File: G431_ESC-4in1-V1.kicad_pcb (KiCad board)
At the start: 4 copper layers, 46 x 55.8 mm, 223 parts, among them J1 Conn_01x02, J10 Conn_01x03, J11 Conn_01x03, J2 Conn_01x10, J3 Conn_01x04, J4 Conn_01x04, J5 Conn_01x04, J6 Conn_01x03, J7 Conn_01x04, J8 Conn_01x03, J9 Conn_01x10, Q1 TPH1R204PB, Q10 TPH1R204PB, Q11 TPH1R204PB, Q12 TPH1R204PB, Q13 TPH1R204PB, Q14 TPH1R204PB, Q15 TPH1R204PB, Q16 TPH1R204PB, Q17 TPH1R204PB, Q18 TPH1R204PB, Q19 TPH1R204PB, Q2 TPH1R204PB, Q20 TPH1R204PB, Q21 TPH1R204PB, Q22 TPH1R204PB, Q23 TPH1R204PB, Q24 TPH1R204PB, Q3 TPH1R204PB, Q4 TPH1R204PB, Q5 TPH1R204PB, Q6 TPH1R204PB, Q7 TPH1R204PB, Q8 TPH1R204PB, Q9 TPH1R204PB, U1 FD6288Q, U10 FD6288Q, U11 FD6288Q, U12 STM32G431KBU6, U13 L78L12_SOT89, U14 MP4560_QFN10, U15 DTOM, U2 STM32G431KBU6, U3 L78L12_SOT89, U4 LP2985-3.3, U5 INA139, U6 STM32G431KBU6, U7 OPA340NA, U8 FD6288Q, U9 STM32G431KBU6

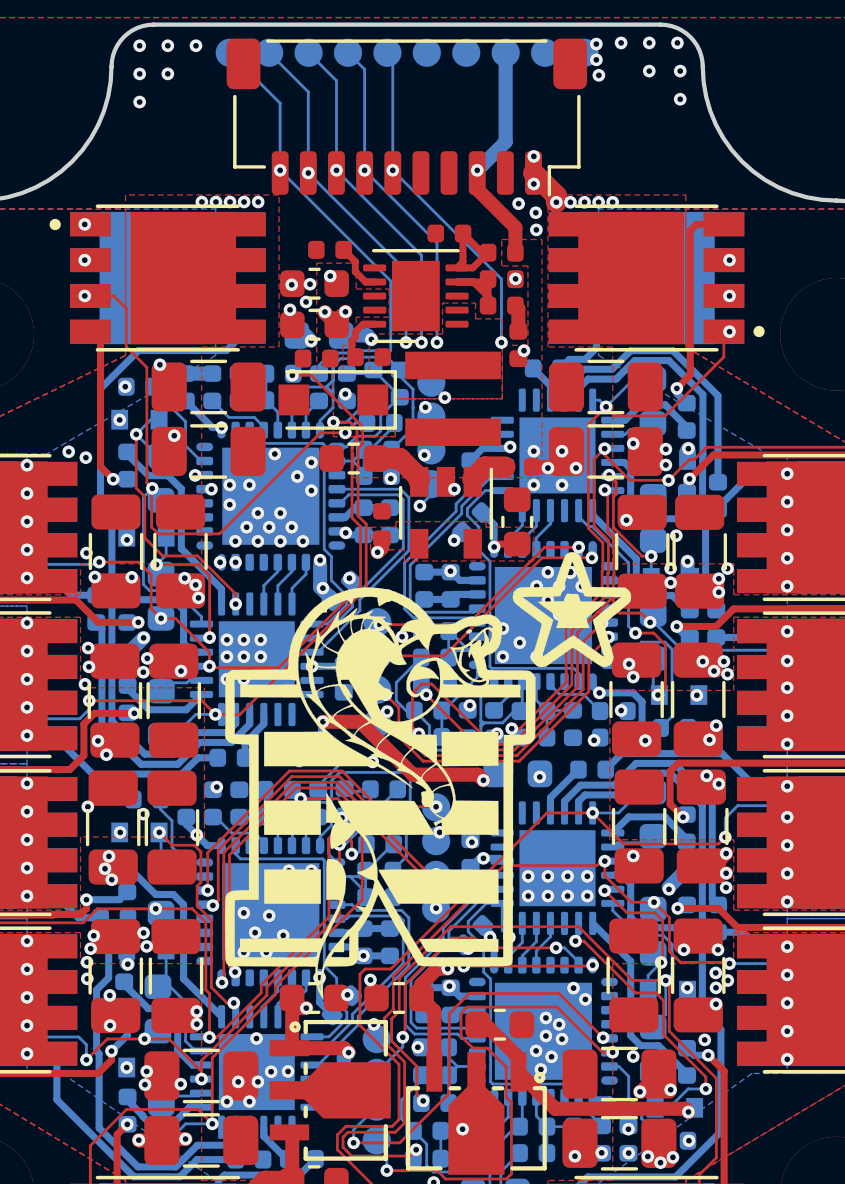
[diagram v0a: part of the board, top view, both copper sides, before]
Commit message: Slight adjustments to Logo and traces
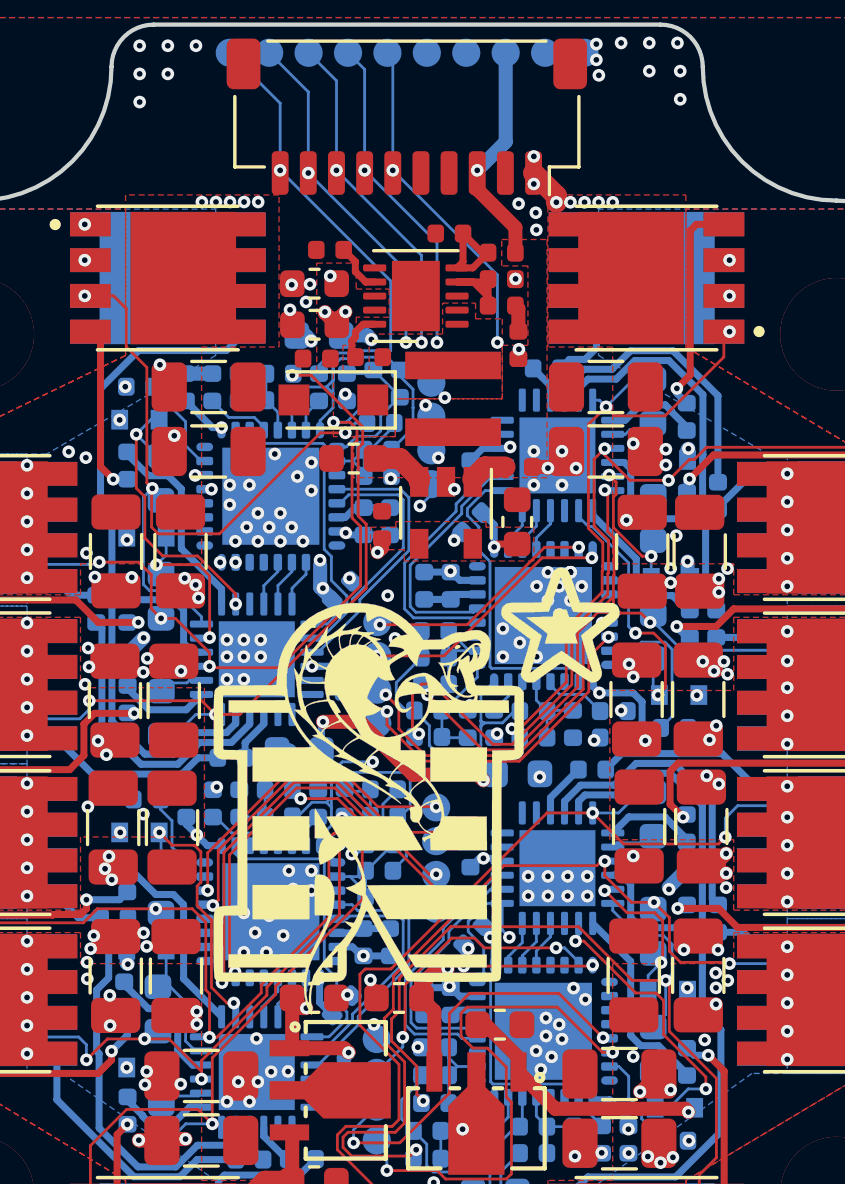
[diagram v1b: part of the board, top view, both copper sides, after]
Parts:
- moved U15 0.69 mm to (140.1, 89.3)
